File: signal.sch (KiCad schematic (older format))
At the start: 30 parts, among them J1 Conn_Coaxial, J2 Screw_Terminal_01x02, J3 AudioJack2_Ground, U1 Si5351A-B-GT, U2 SN74LVC74APW, U3 TS5A23157DGSR, U4 AD8032ANZ, X1 CSX-750FBC25000000T

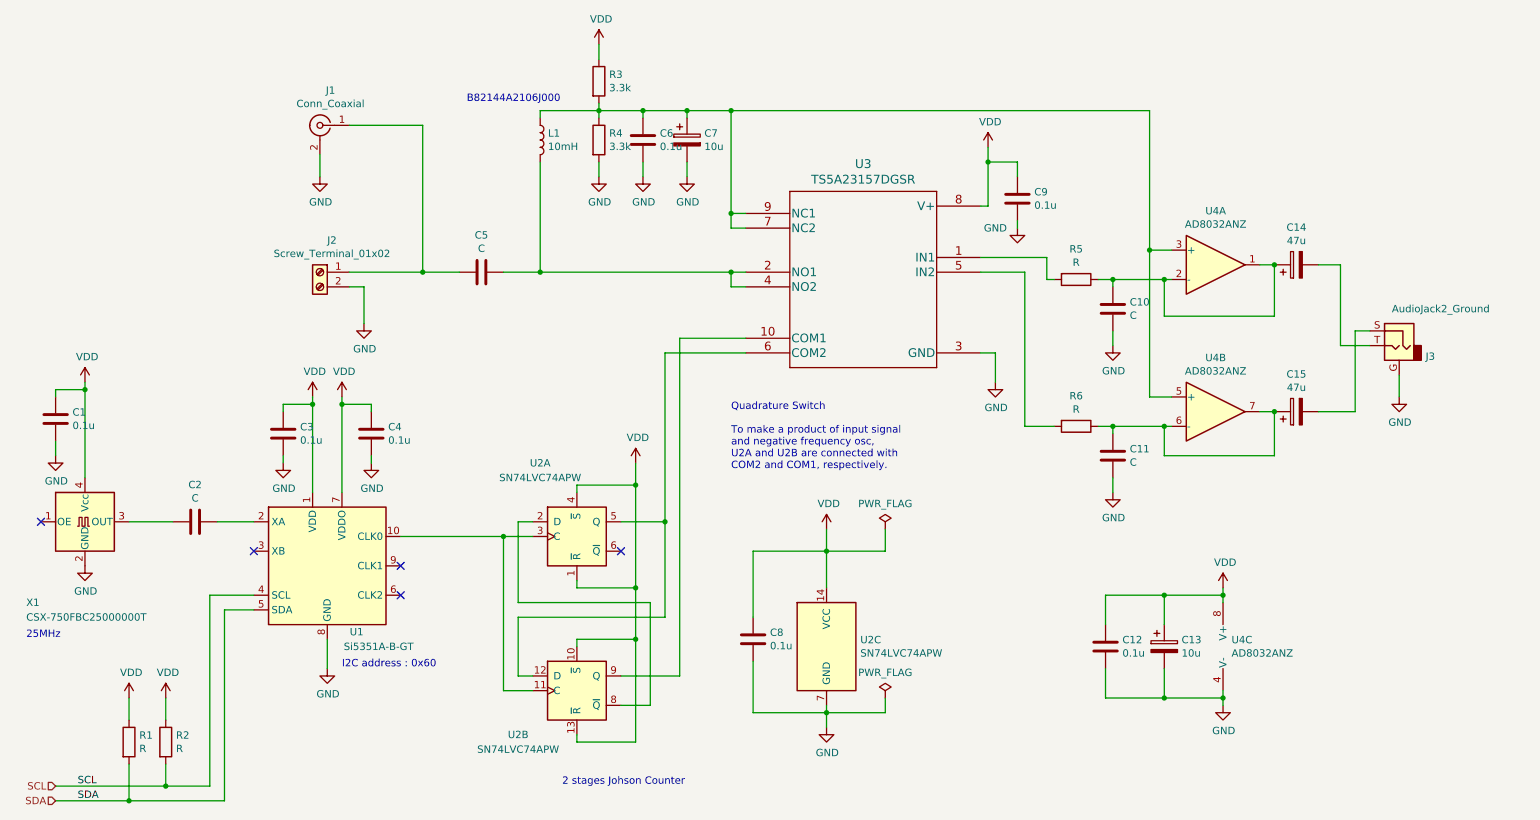
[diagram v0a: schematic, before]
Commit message: Schematics are almost done.
Audio jack is not yet.
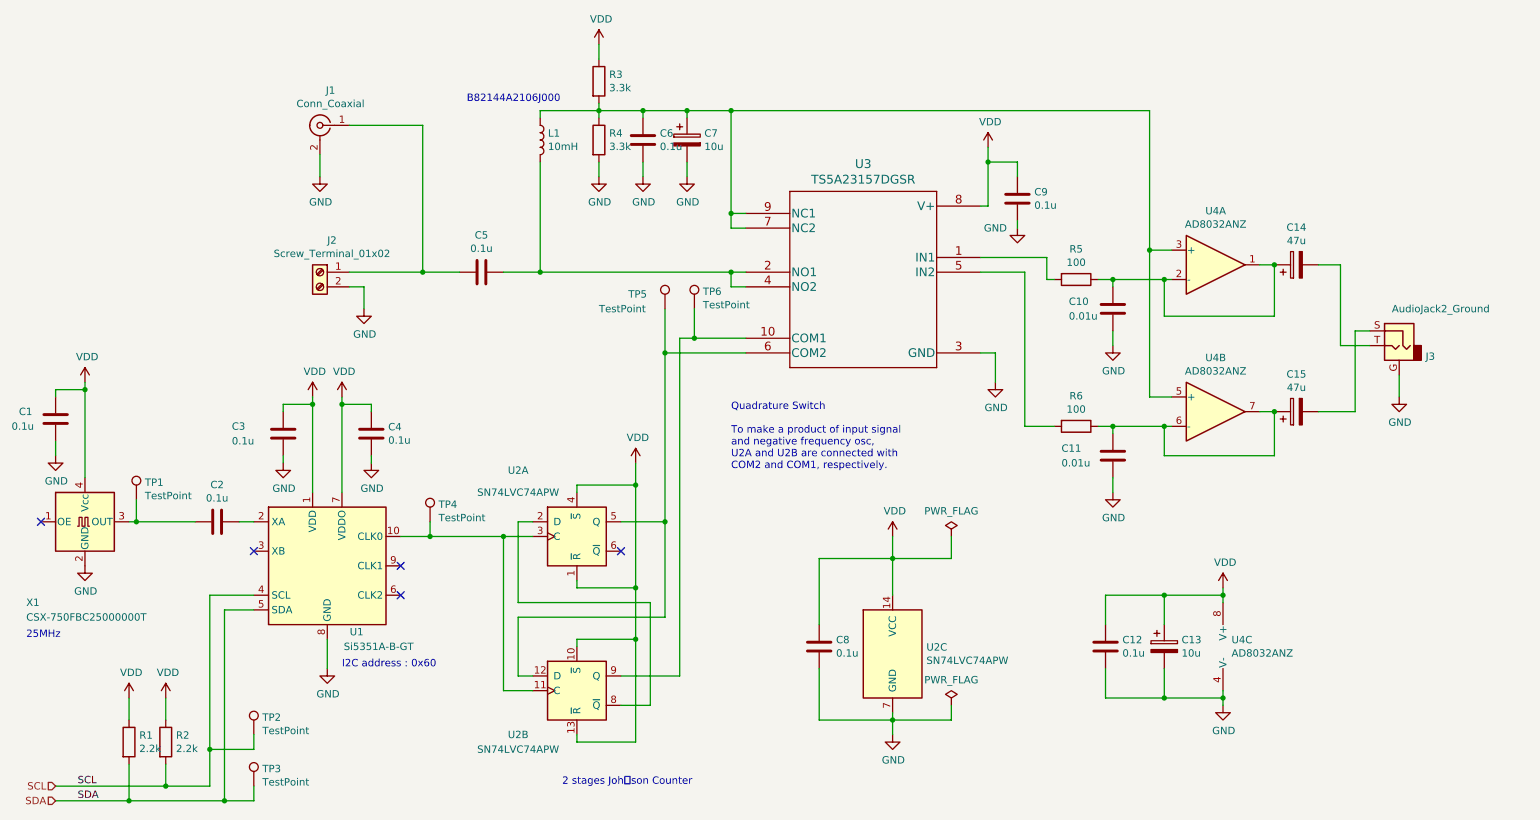
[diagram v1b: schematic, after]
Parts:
- added TP1, TP2, TP3, TP4, TP5, TP6: TestPoint, Measurement_Points:Measurement_Point_Round-TH_Big, symbol Connector:TestPoint
- C1, C12, C3, C4, C6, C8, C9: footprint (none) -> Capacitors_THT:C_Disc_D4.7mm_W2.5mm_P5.00mm
- C10, C11: value C -> 0.01u; footprint (none) -> Capacitors_THT:C_Disc_D4.7mm_W2.5mm_P5.00mm
- C13, C14, C15, C7: footprint (none) -> Capacitors_THT:CP_Radial_D8.0mm_P2.50mm
- C2, C5: value C -> 0.1u; footprint (none) -> Capacitors_THT:C_Disc_D4.7mm_W2.5mm_P5.00mm
- J1: footprint (none) -> Connectors:SMA_THT_Jack_Straight
- J2: footprint (none) -> Connectors_Terminal_Blocks:TerminalBlock_bornier-2_P5.08mm
- L1, R3, R4: footprint (none) -> Resistors_THT:R_Axial_DIN0204_L3.6mm_D1.6mm_P2.54mm_Vertical
- R1, R2: value R -> 2.2k; footprint (none) -> Resistors_THT:R_Axial_DIN0204_L3.6mm_D1.6mm_P2.54mm_Vertical
- R5, R6: value R -> 100; footprint (none) -> Resistors_THT:R_Axial_DIN0204_L3.6mm_D1.6mm_P2.54mm_Vertical
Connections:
- net SCL: now also TP2.1
- net SDA: now also TP3.1
- net at U1.10 (CLK0), U2.11 (C), U2.3 (C): now also TP4.1
- net at C2.2, X1.3 (OUT): now also TP1.1
- net at U2.12 (D), U2.5 (Q), U3.6 (COM2): now also TP5.1
- net at U2.9 (Q), U3.10 (COM1): now also TP6.1
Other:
- note added: "2 stages Johｎson Counter"
- note removed: "2 stages Johson Counter"
- moved on the sheet: C2, C8, U2C

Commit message: Footprint done.
Added footprint of the audio jack.
The documentation link of the each IC is done.
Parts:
- J3: value AudioJack2_Ground -> SJ1-3533; footprint (none) -> project_lib:Jack_3.5mm_CUI_SJ1-3533NG_Horizontal_CircularHoles
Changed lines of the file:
@@
 F 1 "CSX-750FBC25000000T" H 950 3800 50  0000 L CNN
 F 2 "Oscillators:Oscillator_SMD_SeikoEpson_SG8002CA-4pin_7.0x5.0mm_HandSoldering" H 2050 4100 50  0001 C CNN
-F 3 "https://support.epson.biz/td/api/doc_check.php?mode=dl&lang=en&Parts=SG-51P" H 1250 4450 50  0001 C CNN
+F 3 "https://www.digikey.jp/product-detail/ja/citizen-finedevice-co-ltd/CSX-750FBC25000000T/300-7246-1-ND/482134" H 1250 4450 50  0001 C CNN
 	1    1350 4450
 	1    0    0    -1
@@
 F 1 "SN74LVC74APW" H 4300 4850 50  0000 C CNN
 F 2 "Housings_SSOP:TSSOP-14_4.4x5mm_Pitch0.65mm" H 4700 4550 50  0001 C CNN
-F 3 "74xx/74hc_hct74.pdf" H 4700 4550 50  0001 C CNN
+F 3 "https://www.tij.co.jp/product/jp/SN74LVC74A" H 4700 4550 50  0001 C CNN
 	1    4700 4550
 	1    0    0    -1
@@
 F 1 "SN74LVC74APW" H 7080 5305 50  0000 L CNN
 F 2 "Housings_SSOP:TSSOP-14_4.4x5mm_Pitch0.65mm" H 6850 5350 50  0001 C CNN
-F 3 "74xx/74hc_hct74.pdf" H 6850 5350 50  0001 C CNN
+F 3 "https://www.tij.co.jp/product/jp/SN74LVC74A" H 6850 5350 50  0001 C CNN
 	3    6850 5350
 	1    0    0    -1
@@
 F 1 "AD8032ANZ" H 9050 2976 50  0000 C CNN
 F 2 "Housings_DIP:DIP-8_W7.62mm" H 9150 2700 50  0001 C CNN
-F 3 "http://ww1.microchip.com/downloads/en/devicedoc/22140b.pdf" H 9300 2850 50  0001 C CNN
+F 3 "https://www.analog.com/media/en/technical-documentation/data-sheets/AD8031_8032.pdf" H 9300 2850 50  0001 C CNN
 	1    9050 2700
 	1    0    0    -1
@@
 F 1 "AD8032ANZ" H 9050 3976 50  0000 C CNN
 F 2 "Housings_DIP:DIP-8_W7.62mm" H 9150 3700 50  0001 C CNN
-F 3 "http://ww1.microchip.com/downloads/en/devicedoc/22140b.pdf" H 9300 3850 50  0001 C CNN
+F 3 "https://www.analog.com/media/en/technical-documentation/data-sheets/AD8031_8032.pdf" H 9300 3850 50  0001 C CNN
 	2    9050 3700
 	1    0    0    -1
@@
 F 1 "AD8032ANZ" H 9158 5255 50  0000 L CNN
 F 2 "Housings_DIP:DIP-8_W7.62mm" H 9200 5300 50  0001 C CNN
-F 3 "http://ww1.microchip.com/downloads/en/devicedoc/22140b.pdf" H 9350 5450 50  0001 C CNN
+F 3 "https://www.analog.com/media/en/technical-documentation/data-sheets/AD8031_8032.pdf" H 9350 5450 50  0001 C CNN
 	3    9100 5300
 	1    0    0    -1
@@
 F 1 "TS5A23157DGSR" H 6650 2881 60  0000 C CNN
 F 2 "project_lib:TS5A23157DGSR" H 6650 2840 60  0001 C CNN
-F 3 "" H 5850 2500 60  0000 C CNN
+F 3 "https://www.tij.co.jp/product/jp/TS5A23157" H 5850 2500 60  0000 C CNN
 	1    5850 2500
 	1    0    0    -1
@@
 P 10300 3250
 F 0 "J3" H 10120 3176 50  0000 R CNN
-F 1 "AudioJack2_Ground" H 10350 3500 50  0000 R CNN
-F 2 "" H 10300 3250 50  0001 C CNN
-F 3 "~" H 10300 3250 50  0001 C CNN
+F 1 "SJ1-3533" H 10350 3500 50  0000 R CNN
+F 2 "project_lib:Jack_3.5mm_CUI_SJ1-3533NG_Horizontal_CircularHoles" H 10300 3250 50  0001 C CNN
+F 3 "https://www.digikey.jp/product-detail/ja/cui-devices/SJ1-3533/CP1-3533-ND/738695" H 10300 3250 50  0001 C CNN
 	1    10300 3250
 	-1   0    0    -1
@@
 F 1 "SN74LVC74APW" H 4300 5200 50  0000 C CNN
 F 2 "Housings_SSOP:TSSOP-14_4.4x5mm_Pitch0.65mm" H 4700 5600 50  0001 C CNN
-F 3 "74xx/74hc_hct74.pdf" H 4700 5600 50  0001 C CNN
+F 3 "https://www.tij.co.jp/product/jp/SN74LVC74A" H 4700 5600 50  0001 C CNN
 	2    4700 5600
 	1    0    0    -1

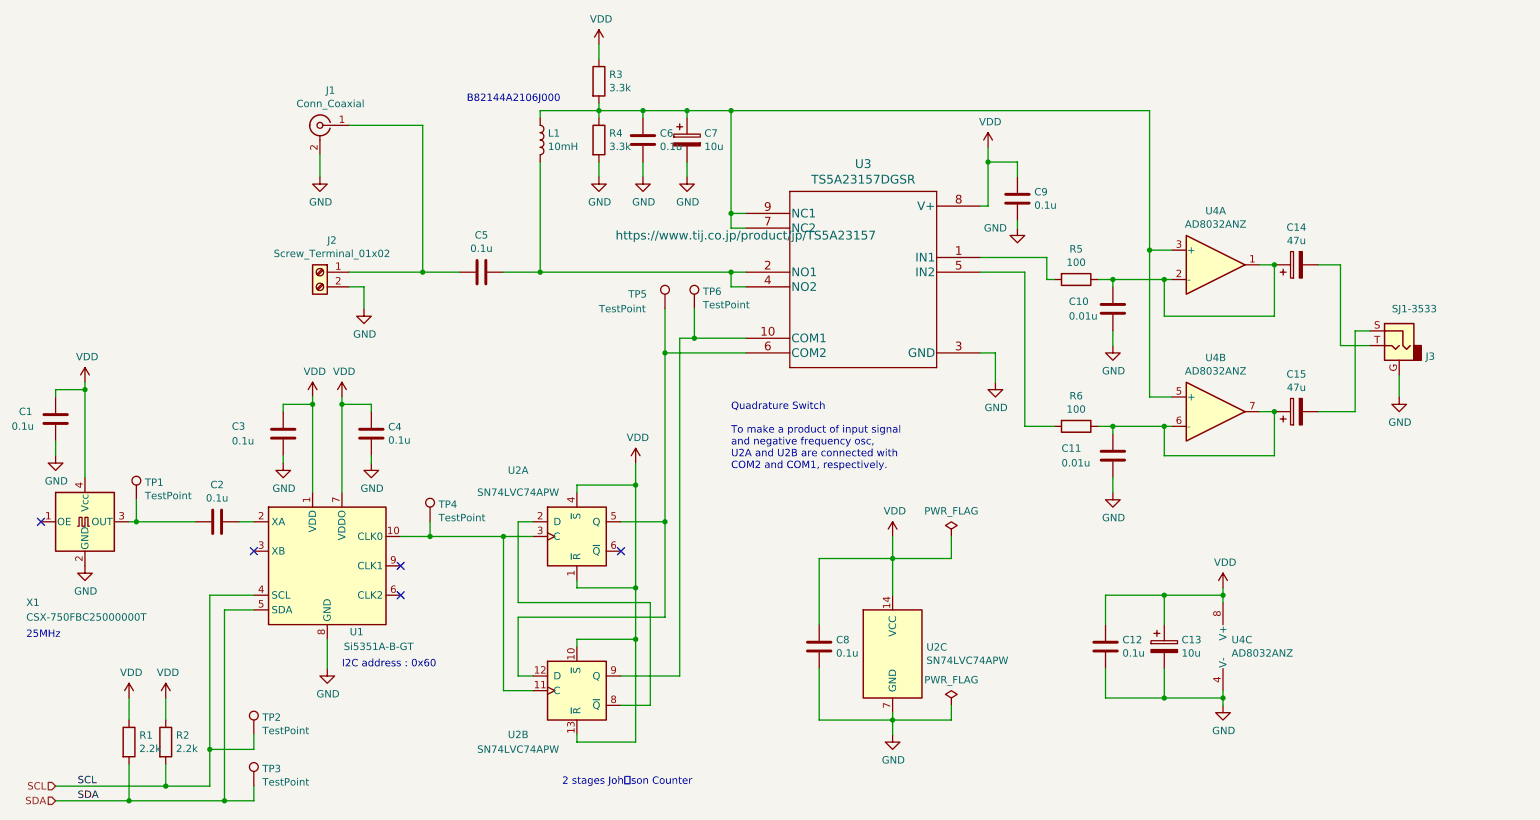
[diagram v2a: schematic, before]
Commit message: All parts is on the PCB.
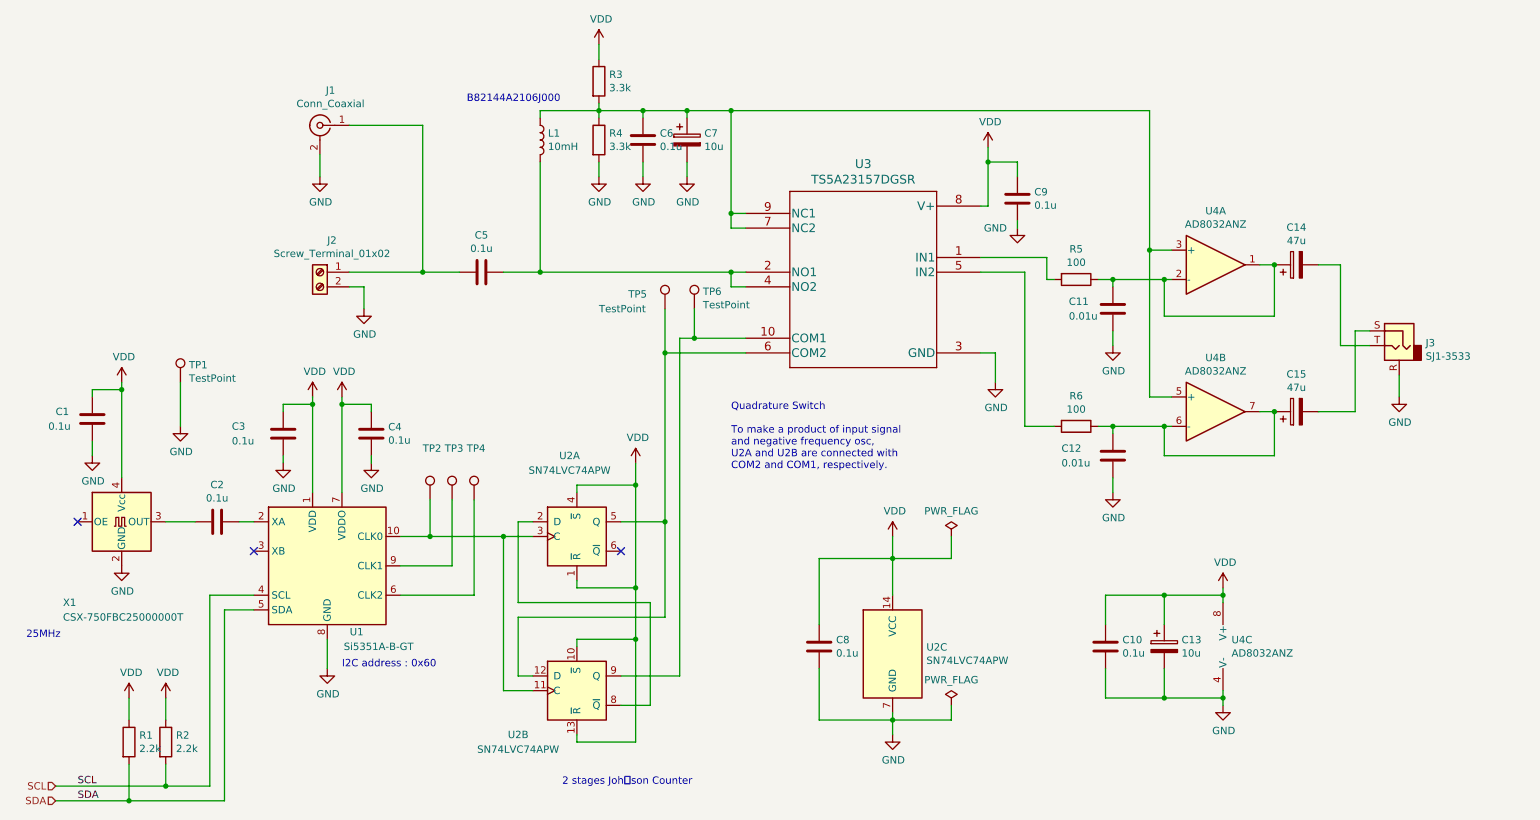
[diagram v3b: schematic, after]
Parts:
- removed J3: SJ1-3533, project_lib:Jack_3.5mm_CUI_SJ1-3533NG_Horizontal_CircularHoles, symbol Connector:AudioJack2_Ground
- removed TP2: TestPoint, Measurement_Points:Measurement_Point_Round-TH_Big, symbol Connector:TestPoint
- added J3: SJ1-3533, project_lib:Jack_3.5mm_CUI_SJ1-3533NG_Horizontal_CircularHoles, symbol SJ1-3533:SJ1-3533
- added TP4: TestPoint, Measurement_Points:Measurement_Point_Round-TH_Big, symbol Connector:TestPoint
- renumbered C12 to C10, C10 to C11, C11 to C12, TP4 to TP2
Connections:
- net GND: now also TP1.1, J3.R
- net SDA: no longer TP3.1
- net at U1.6 (CLK2): now also TP4.1
- net at U1.9 (CLK1): now also TP3.1
- net at C2.2, X1.3 (OUT): no longer TP1.1
- net at C15.2: now also J3.S
- net at C14.2: now also J3.T
- no-connect marks 5 -> 3
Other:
- moved on the sheet: C1, TP1, TP2, X1

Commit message: Added jumper to short the op-amp.
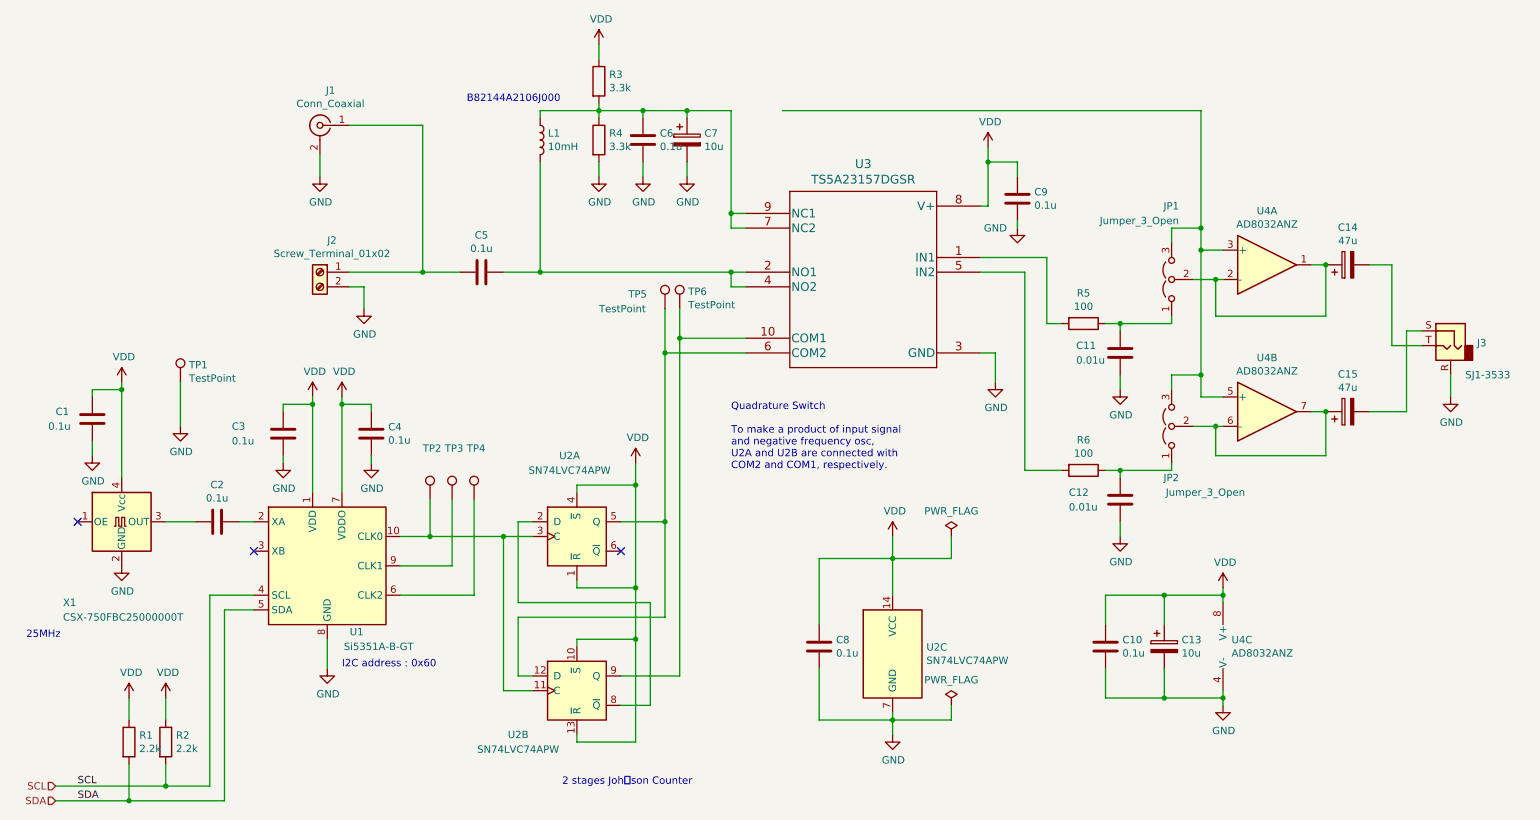
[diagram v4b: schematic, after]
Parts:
- added JP1, JP2: Jumper_3_Open, Pin_Headers:Pin_Header_Straight_1x03_Pitch2.54mm, symbol Jumper:Jumper_3_Open
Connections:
- net at C14.1, U4.1, U4.2 (-): now also JP1.2 (C); no longer C11.1, R5.1
- net at C6.1, C7.1, L1.1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: no longer U4.3 (+), U4.5 (+)
- net at C15.1, U4.6 (-), U4.7: now also JP2.2 (C); no longer C12.1, R6.1
- new net: JP1.3 (B), JP2.3 (B), U4.3 (+), U4.5 (+)
- new net: C11.1, JP1.1 (A), R5.1
- new net: C12.1, JP2.1 (A), R6.1
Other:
- moved on the sheet: C11, C12, C14, C15, J3, R5, R6, TP6, U4A, U4B
